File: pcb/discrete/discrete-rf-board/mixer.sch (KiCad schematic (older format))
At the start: 50 parts, among them J1401 Conn_Coaxial, Q1401 Q_NPN_BCE, Q1402 Q_NPN_BCE, Q1403 Q_NPN_BCE, Q1404 Q_PNP_BCE, Q1405 Q_PNP_BCE, Q1406 Q_NPN_BCE, Q1407 Q_NPN_BCE, U1401 LT5560EDD#PBF

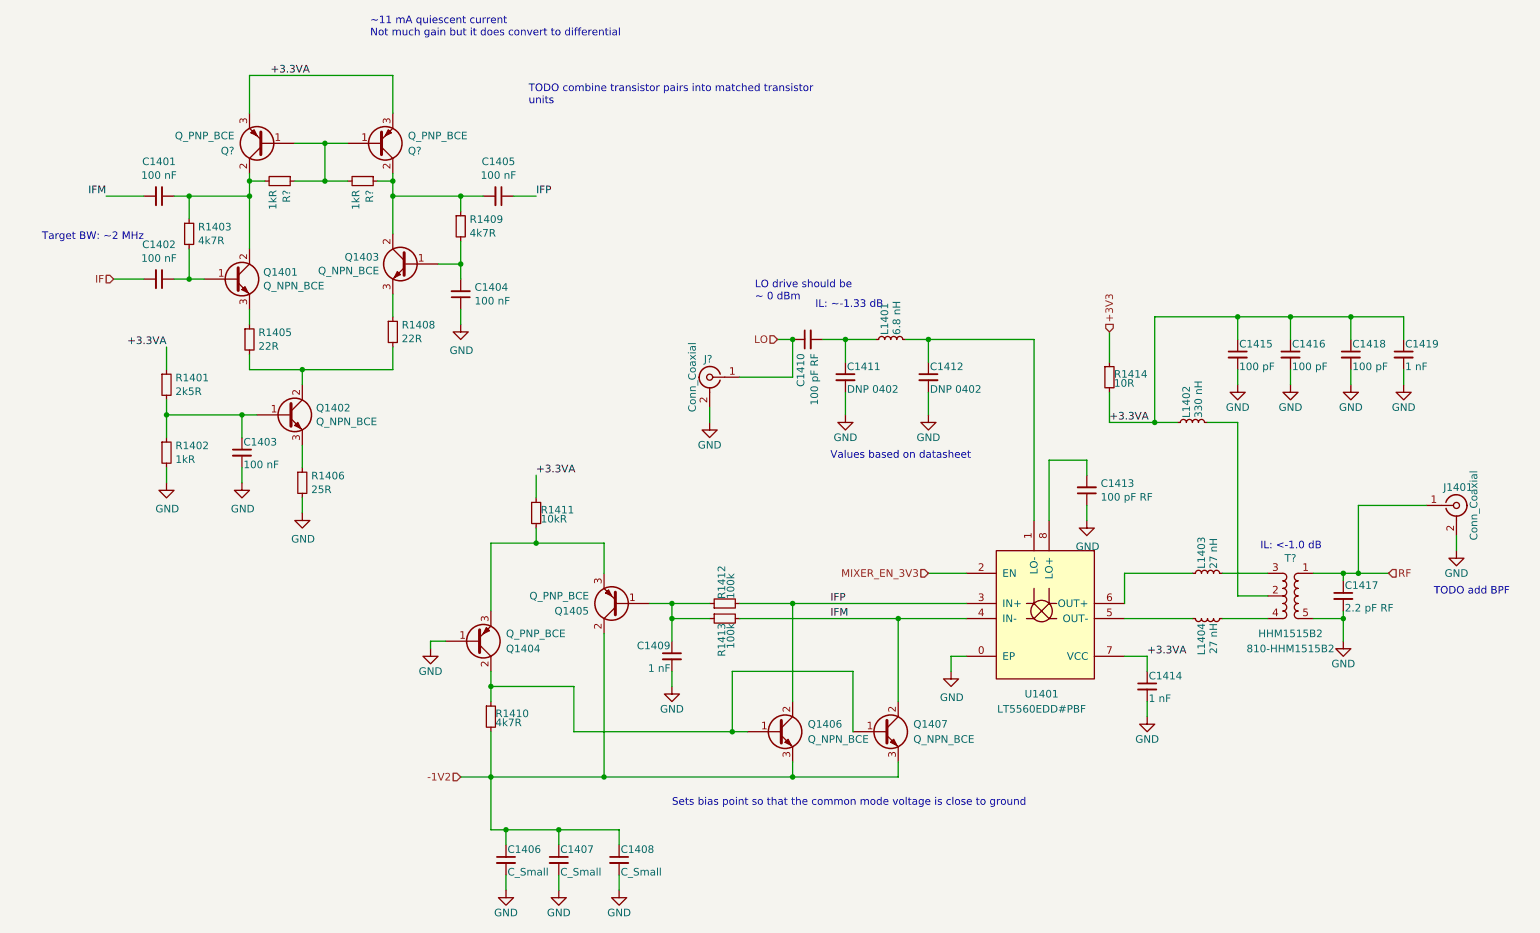
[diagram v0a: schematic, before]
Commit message: Design DAC/ADC stages, pass out all control signals to top sheet
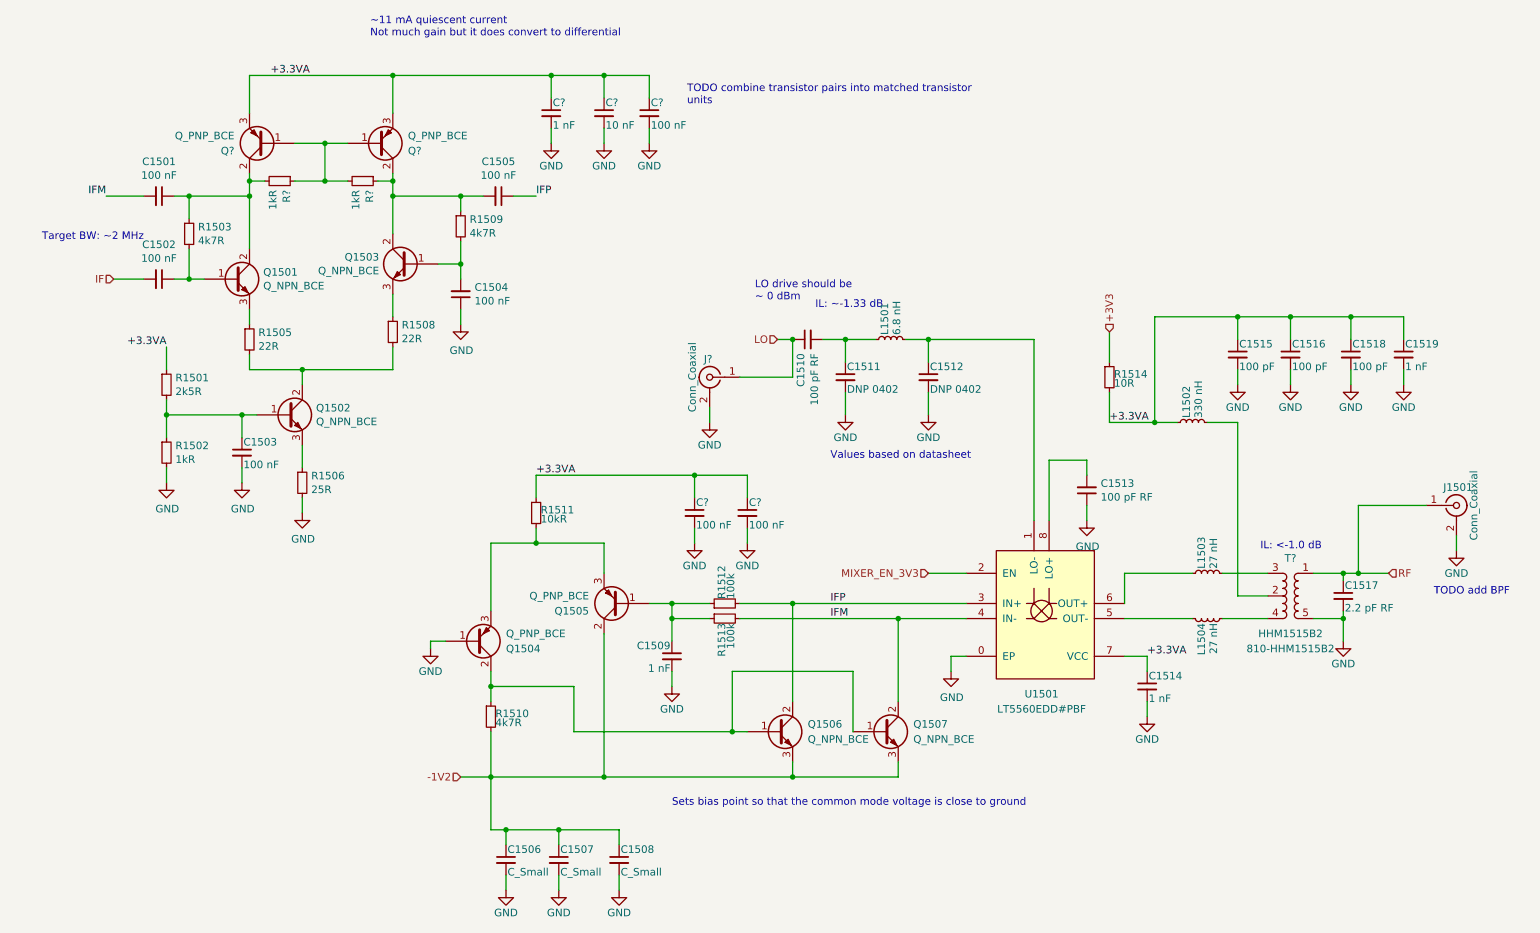
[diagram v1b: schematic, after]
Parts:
- added C?: 1 nF, symbol Device:C_Small
- added C?: 10 nF, symbol Device:C_Small
- added C? (x3): 100 nF, symbol Device:C_Small
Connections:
- net +3.3VA: now also C?.1, C?.1, C?.1, C?.1, C?.1
- net GND: now also C?.2, C?.2, C?.2, C?.2, C?.2

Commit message: Wire out all control signals to connectors TODO PLL charge pump loop, bypass caps in attenuator circuit, antialiasing filter for ADC frontend
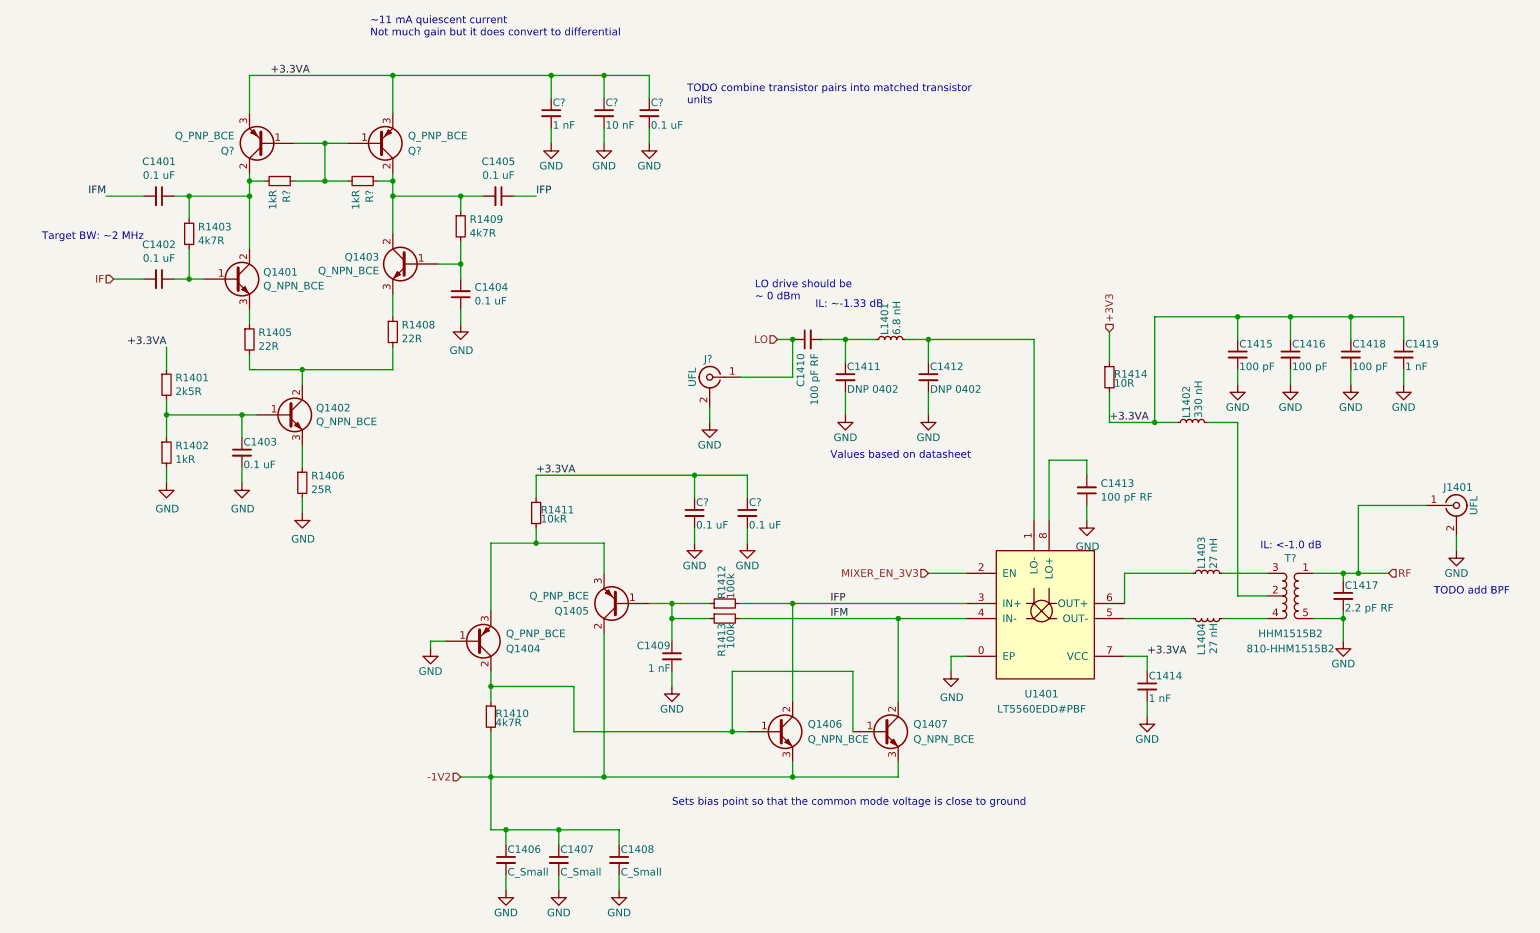
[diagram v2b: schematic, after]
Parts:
- C1401, C1402, C1403, C1404, C1405, C? (x3): value 100 nF -> 0.1 uF
- J1401, J?: value Conn_Coaxial -> UFL

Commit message: Start work in footprinting everything
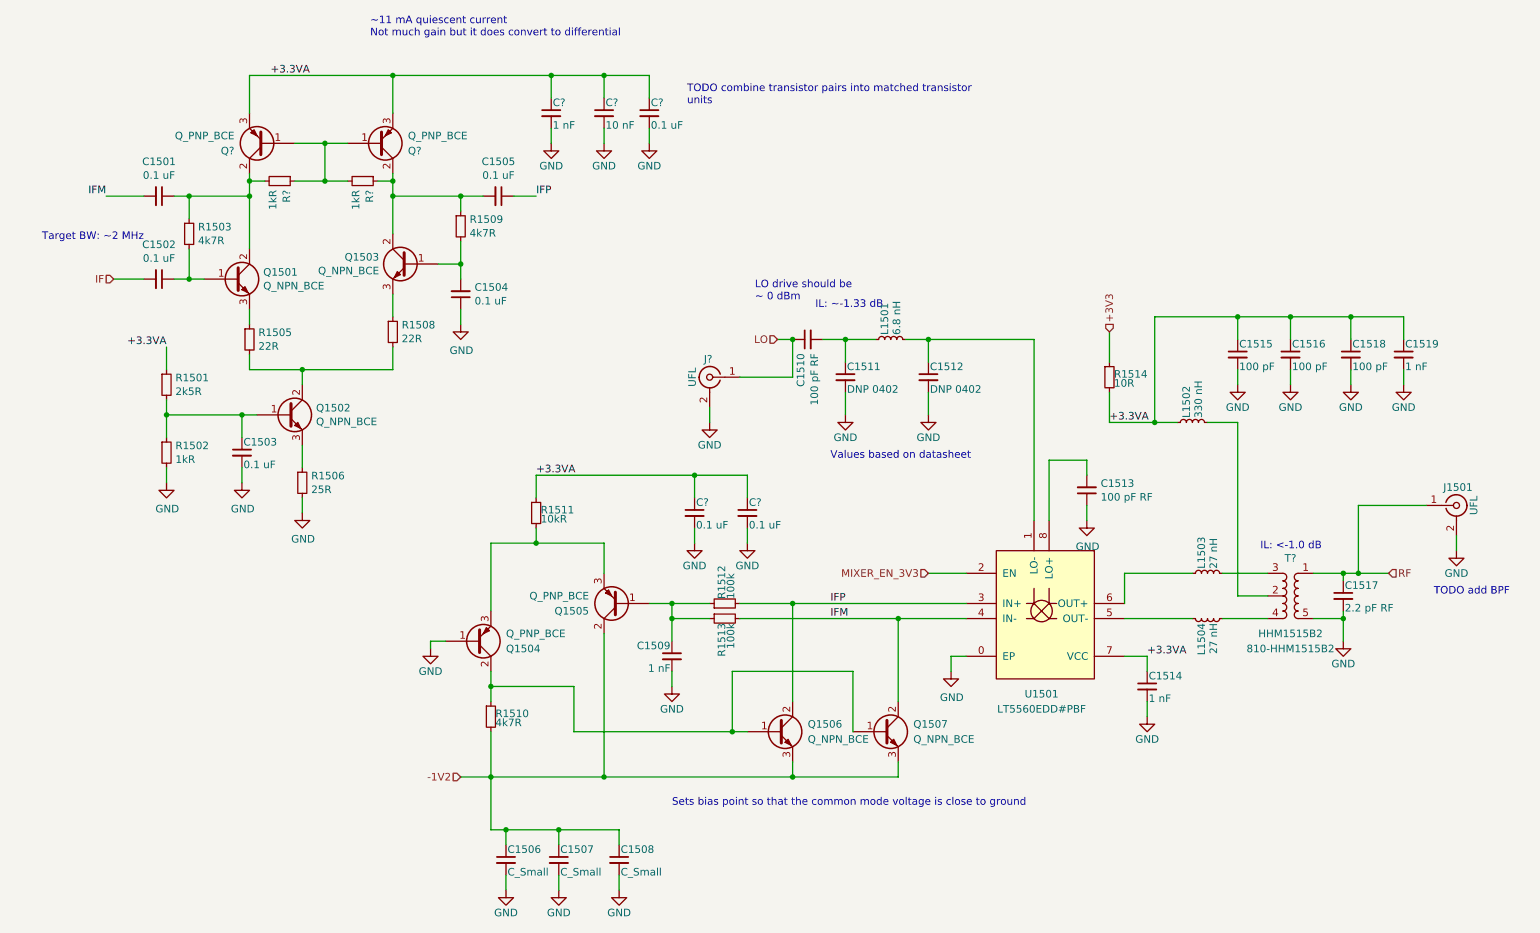
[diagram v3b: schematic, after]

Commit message: The footprintening continues
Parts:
- T?: footprint (none) -> discrete_footprints:TDK_HHM1515B2
- U1401: footprint (none) -> discrete_footprints:Analog_DFN8-EP

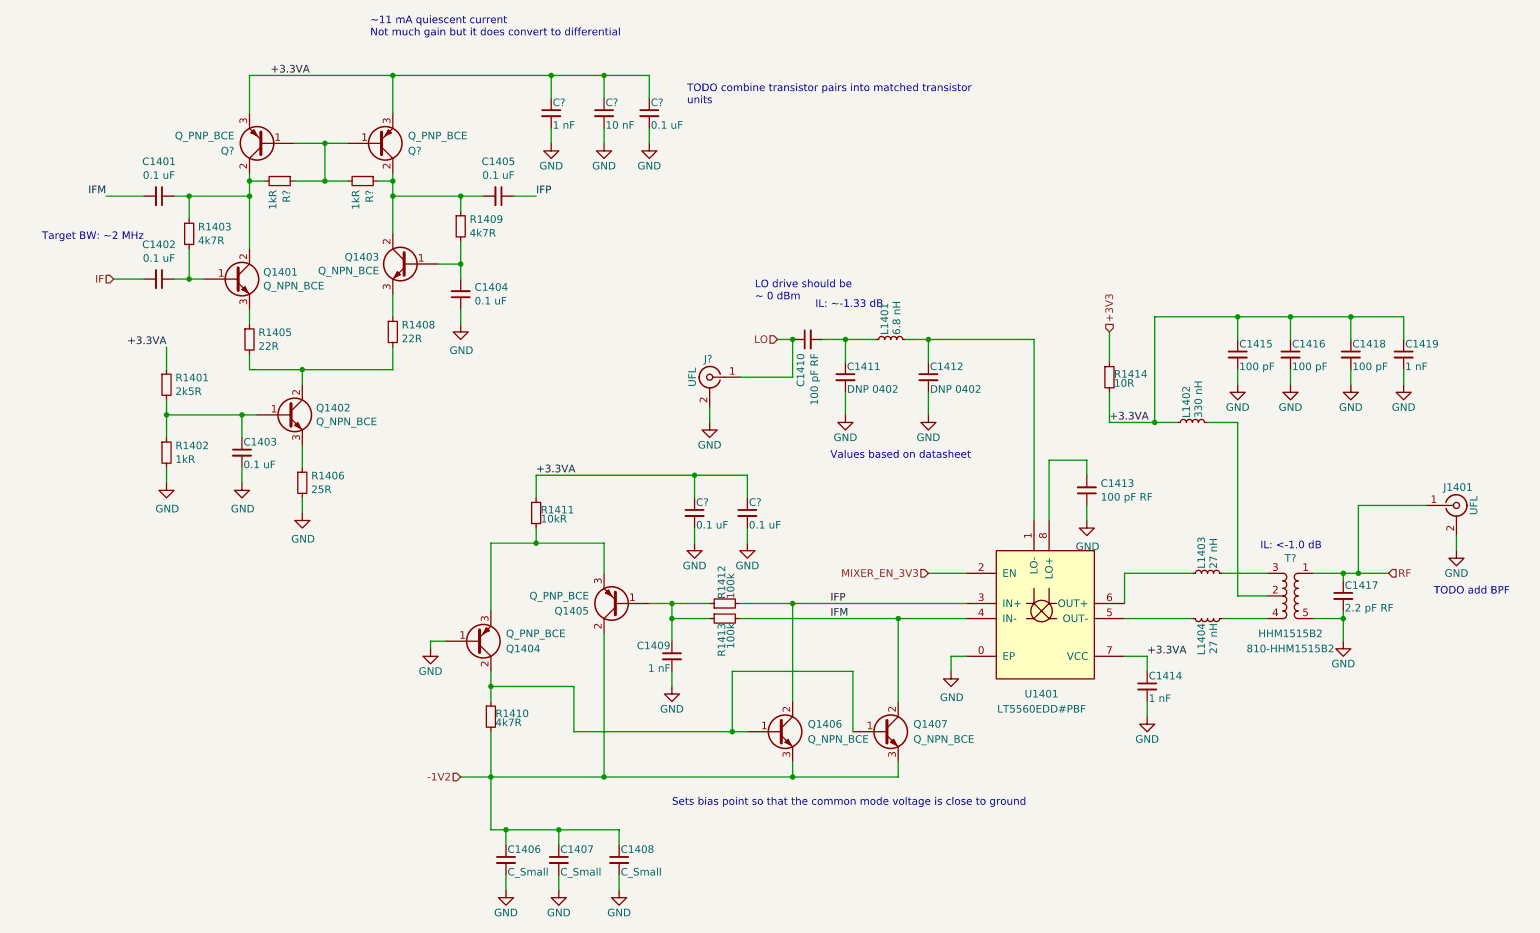
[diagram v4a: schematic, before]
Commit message: Add matching PNP/NPN transistor pairs, fix pin numbering for BFU520R transistors TODO fix biasing on power stage, source last NPN transistor, autofill and start sourcing passives
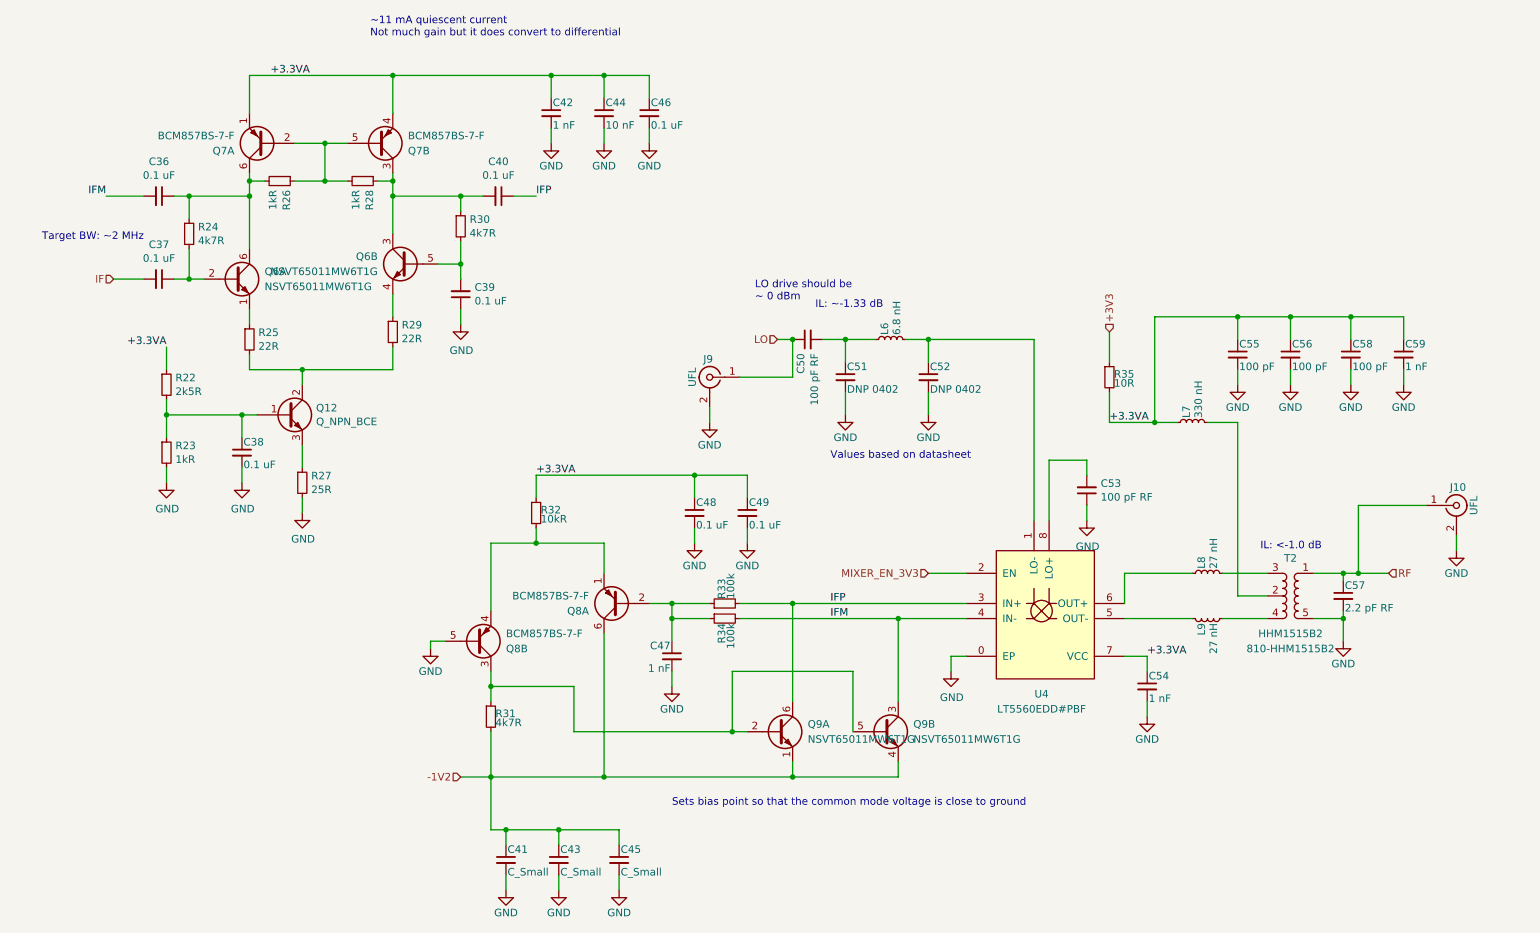
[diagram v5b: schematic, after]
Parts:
- removed Q1401, Q1403, Q1406, Q1407: Q_NPN_BCE, symbol Device:Q_NPN_BCE
- removed Q1404, Q1405, Q? (x2): Q_PNP_BCE, symbol Device:Q_PNP_BCE
- added Q1, Q5: NSVT65011MW6T1G, Package_TO_SOT_SMD:SOT-363_SC-70-6_Handsoldering, symbol Device:Q_DUAL_NPN_NPN_E1B1C2E2B2C1
- added Q2, Q4: BCM857BS-7-F, Package_TO_SOT_SMD:SOT-363_SC-70-6_Handsoldering, symbol Device:Q_DUAL_PNP_PNP_E1B1C2E2B2C1
- gave numbers to parts that had none: 9
- renumbered C1401 to C12, C1402 to C13, C1403 to C14, C1404 to C15, C1405 to C16, C1406 to C17, C1407 to C19, C1408 to C21, C1409 to C23, C1410 to C26, C1411 to C27, C1412 to C28, C1413 to C29, C1414 to C30, C1415 to C31, C1416 to C32, C1417 to C33, C1418 to C34, C1419 to C35, J1401 to J8, L1401 to L2, L1402 to L3, L1403 to L4, L1404 to L5, Q1402 to Q3, R1403 to R10, R1405 to R11, R1406 to R13, R1408 to R15, R1409 to R16, R1410 to R17, R1411 to R18, R1412 to R19, R1413 to R20, R1414 to R21, R1401 to R8, R1402 to R9, U1401 to U3
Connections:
- net +3.3VA: now also Q2.1 (E1), Q2.4 (E2)
- net -1V2: now also Q4.6 (C1), Q5.1 (E1), Q5.4 (E2)
- net GND: now also Q4.5 (B2)
- net IFM: now also Q5.3 (C2)
- net IFP: now also Q5.6 (C1)
- net at C13.1, R10.2: now also Q1.2 (B1)
- net at C12.1, R10.1, R12.2: now also Q1.6 (C1), Q2.6 (C1)
- net at R11.1: now also Q1.1 (E1)
- net at C15.2, R16.2: now also Q1.5 (B2)
- net at C16.2, R14.1, R16.1: now also Q1.3 (C2), Q2.3 (C2)
- net at R15.1: now also Q1.4 (E2)
- net at R17.1: now also Q4.3 (C2), Q5.2 (B1), Q5.5 (B2)
- net at C23.1, R19.1, R20.1: now also Q4.2 (B1)
- net at R18.2: now also Q4.1 (E1), Q4.4 (E2)
- net at R12.1, R14.2: now also Q2.2 (B1), Q2.5 (B2)
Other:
- note removed: "TODO add BPF"
- note removed: "TODO combine transistor pairs into matched transistor\nunits"
